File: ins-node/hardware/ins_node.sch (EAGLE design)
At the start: 11 parts, among them Q3 MOSFET-2N7000, U1 TINY85-20-DIP

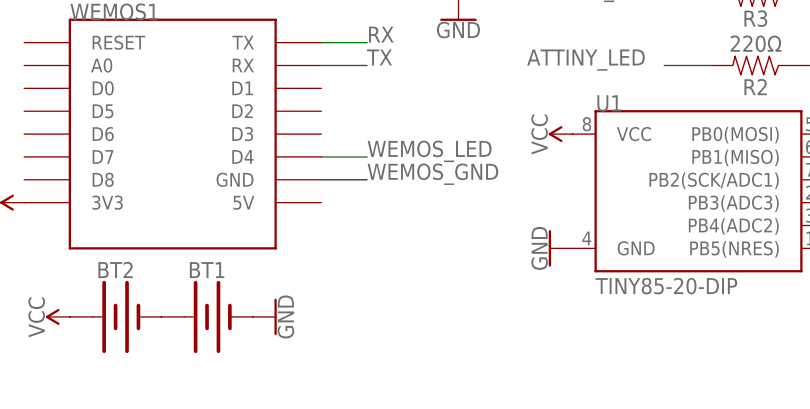
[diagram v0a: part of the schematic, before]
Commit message: Add decoupling capacitor
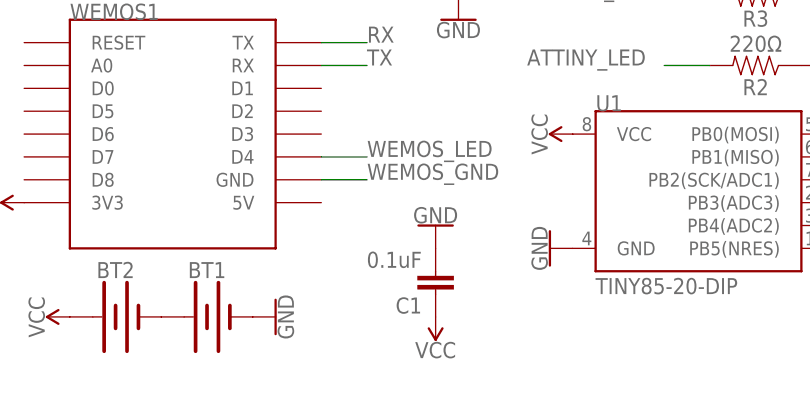
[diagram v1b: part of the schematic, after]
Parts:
- added C1: 0.1uF, SparkFun-Capacitors:0.1UF-KIT-EZ-50V-20%
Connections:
- net GND: now also C1.2
- net VCC: now also C1.1
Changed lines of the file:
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@@
 <part name="D2" library="SparkFun-LED" library_urn="urn:adsk.eagle:library:529" deviceset="LED" device="5MM-KIT" package3d_urn="urn:adsk.eagle:package:39357/1"/>
 <part name="GND5" library="SparkFun-PowerSymbols" library_urn="urn:adsk.eagle:library:530" deviceset="GND" device=""/>
+<part name="C1" library="SparkFun-Capacitors" library_urn="urn:adsk.eagle:library:510" deviceset="0.1UF" device="-KIT-EZ-50V-20%" package3d_urn="urn:adsk.eagle:package:37428/1" value="0.1uF"/>
+<part name="GND6" library="SparkFun-PowerSymbols" library_urn="urn:adsk.eagle:library:530" deviceset="GND" device=""/>
+<part name="SUPPLY5" library="SparkFun-PowerSymbols" library_urn="urn:adsk.eagle:library:530" deviceset="VCC" device=""/>
 </parts>
 <sheets>
@@
 <instance part="D2" gate="G$1" x="116.84" y="58.42" rot="R90"/>
 <instance part="GND5" gate="1" x="129.54" y="58.42" rot="R90"/>
+<instance part="C1" gate="G$1" x="73.66" y="35.56" rot="R180"/>
+<instance part="GND6" gate="1" x="73.66" y="40.64" rot="R180"/>
+<instance part="SUPPLY5" gate="G$1" x="73.66" y="30.48" rot="R180"/>
 </instances>
 <busses>
@@
 <wire x1="127" y1="58.42" x2="121.92" y2="58.42" width="0.1524" layer="91"/>
 </segment>
+<segment>
+<pinref part="C1" gate="G$1" pin="2"/>
+<pinref part="GND6" gate="1" pin="GND"/>
+</segment>
 </net>
 <net name="VCC" class="0">
@@
 <pinref part="SUPPLY4" gate="G$1" pin="VCC"/>
 </segment>
+<segment>
+<pinref part="C1" gate="G$1" pin="1"/>
+<pinref part="SUPPLY5" gate="G$1" pin="VCC"/>
+</segment>
 </net>

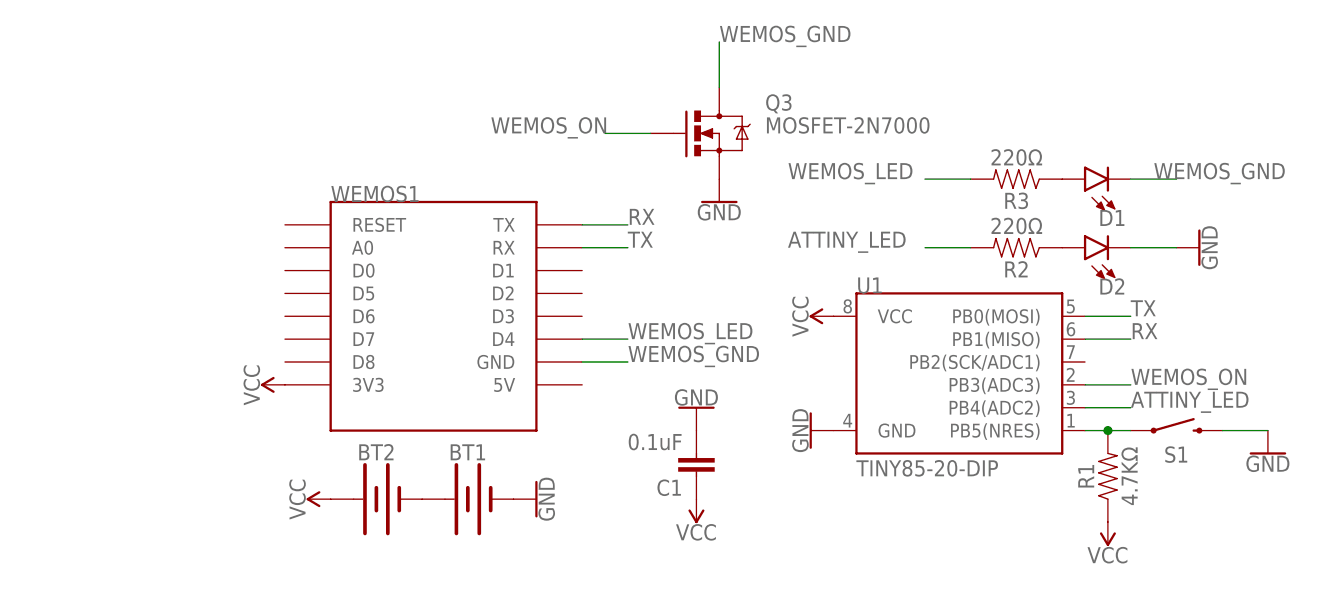
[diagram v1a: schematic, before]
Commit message: Fix wifi module powering issues
HW rev.1 includes:
* 2 MOSFETs for driving the wifi module
* 3 AAA batteries
* Additional decoupling capacitor
* Board restructuring as a result of new components

Fixes #29
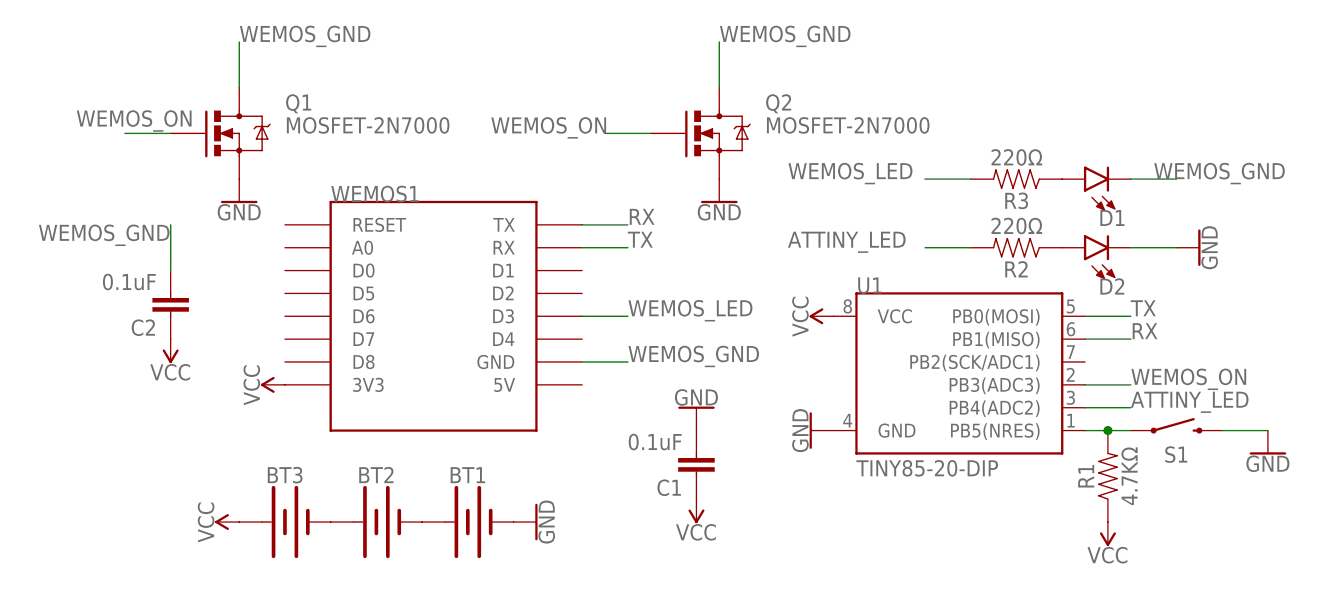
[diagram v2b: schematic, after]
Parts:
- added BT3: (no value), SparkFun-Batteries:BATTERY-AAA
- added C2: 0.1uF, SparkFun-Capacitors:0.1UF-KIT-EZ-50V-20%
- added Q1: MOSFET-2N7000, SparkFun-DiscreteSemi:MOSFET-NCHANNEL2N7000
- renumbered Q3 to Q2
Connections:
- new net N$5: BT2.+, BT3.-
- net GND: now also Q1.S
- net VCC: now also BT3.+, C2.1; no longer BT2.+
- net WEMOS_GND: now also C2.2, Q1.D
- net WEMOS_LED: now also WEMOS1.D3; no longer WEMOS1.D4
- net WEMOS_ON: now also Q1.G
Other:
- moved on the sheet: BT1, BT2
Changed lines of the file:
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@@
 <part name="WEMOS1" library="esp8266modules" deviceset="WEMOS-D1-MINI" device=""/>
 <part name="U1" library="SparkFun-Retired" library_urn="urn:adsk.eagle:library:533" deviceset="ATTINY45" device="TINY85-20-DIP" value="TINY85-20-DIP"/>
-<part name="Q3" library="SparkFun-DiscreteSemi" deviceset="MOSFET-NCHANNEL" device="2N7000" value="MOSFET-2N7000"/>
+<part name="Q2" library="SparkFun-DiscreteSemi" deviceset="MOSFET-NCHANNEL" device="2N7000" value="MOSFET-2N7000"/>
 <part name="BT2" library="SparkFun-Batteries" library_urn="urn:adsk.eagle:library:508" deviceset="BATTERY" device="-AAA" package3d_urn="urn:adsk.eagle:package:37212/1"/>
 <part name="BT1" library="SparkFun-Batteries" library_urn="urn:adsk.eagle:library:508" deviceset="BATTERY" device="-AAA" package3d_urn="urn:adsk.eagle:package:37212/1"/>
@@
 <part name="GND6" library="SparkFun-PowerSymbols" library_urn="urn:adsk.eagle:library:530" deviceset="GND" device=""/>
 <part name="SUPPLY5" library="SparkFun-PowerSymbols" library_urn="urn:adsk.eagle:library:530" deviceset="VCC" device=""/>
+<part name="BT3" library="SparkFun-Batteries" library_urn="urn:adsk.eagle:library:508" deviceset="BATTERY" device="-AAA" package3d_urn="urn:adsk.eagle:package:37212/1"/>
+<part name="Q1" library="SparkFun-DiscreteSemi" deviceset="MOSFET-NCHANNEL" device="2N7000" value="MOSFET-2N7000"/>
+<part name="GND7" library="SparkFun-PowerSymbols" library_urn="urn:adsk.eagle:library:530" deviceset="GND" device=""/>
+<part name="C2" library="SparkFun-Capacitors" library_urn="urn:adsk.eagle:library:510" deviceset="0.1UF" device="-KIT-EZ-50V-20%" package3d_urn="urn:adsk.eagle:package:37428/1" value="0.1uF"/>
+<part name="SUPPLY6" library="SparkFun-PowerSymbols" library_urn="urn:adsk.eagle:library:530" deviceset="VCC" device=""/>
 </parts>
 <sheets>
@@
 <instance part="WEMOS1" gate="D1" x="43.18" y="50.8"/>
 <instance part="U1" gate="G$1" x="104.14" y="43.18"/>
-<instance part="Q3" gate="G$1" x="76.2" y="71.12"/>
-<instance part="BT2" gate="G$1" x="38.1" y="30.48"/>
-<instance part="BT1" gate="G$1" x="48.26" y="30.48"/>
-<instance part="GND1" gate="1" x="55.88" y="30.48" rot="R90"/>
+<instance part="Q2" gate="G$1" x="76.2" y="71.12"/>
+<instance part="BT2" gate="G$1" x="38.1" y="27.94"/>
+<instance part="BT1" gate="G$1" x="48.26" y="27.94"/>
+<instance part="GND1" gate="1" x="55.88" y="27.94" rot="R90"/>
 <instance part="GND2" gate="1" x="76.2" y="63.5"/>
 <instance part="GND3" gate="1" x="86.36" y="38.1" rot="R270"/>
-<instance part="SUPPLY1" gate="G$1" x="33.02" y="30.48" rot="R90"/>
+<instance part="SUPPLY1" gate="G$1" x="22.86" y="27.94" rot="R90"/>
 <instance part="SUPPLY2" gate="G$1" x="27.94" y="43.18" rot="R90"/>
 <instance part="SUPPLY3" gate="G$1" x="88.9" y="50.8" rot="R90"/>
@@
 <instance part="GND6" gate="1" x="73.66" y="40.64" rot="R180"/>
 <instance part="SUPPLY5" gate="G$1" x="73.66" y="30.48" rot="R180"/>
+<instance part="BT3" gate="G$1" x="27.94" y="27.94"/>
+<instance part="Q1" gate="G$1" x="22.86" y="71.12"/>
+<instance part="GND7" gate="1" x="22.86" y="63.5"/>
+<instance part="C2" gate="G$1" x="15.24" y="53.34" rot="R180"/>
+<instance part="SUPPLY6" gate="G$1" x="15.24" y="48.26" rot="R180"/>
 </instances>
 <busses>
@@
 </segment>
 <segment>
-<pinref part="Q3" gate="G$1" pin="S"/>
+<pinref part="Q2" gate="G$1" pin="S"/>
 <pinref part="GND2" gate="1" pin="GND"/>
 </segment>
@@
 <pinref part="GND6" gate="1" pin="GND"/>
 </segment>
+<segment>
+<pinref part="Q1" gate="G$1" pin="S"/>
+<pinref part="GND7" gate="1" pin="GND"/>
+</segment>
 </net>
 <net name="VCC" class="0">
-<segment>
-<pinref part="BT2" gate="G$1" pin="+"/>
-<pinref part="SUPPLY1" gate="G$1" pin="VCC"/>
-</segment>
 <segment>
 <pinref part="WEMOS1" gate="D1" pin="3V3"/>
@@
 <pinref part="C1" gate="G$1" pin="1"/>
 <pinref part="SUPPLY5" gate="G$1" pin="VCC"/>
+</segment>
+<segment>
+<pinref part="SUPPLY1" gate="G$1" pin="VCC"/>
+<pinref part="BT3" gate="G$1" pin="+"/>
+</segment>
+<segment>
+<pinref part="C2" gate="G$1" pin="1"/>
+<pinref part="SUPPLY6" gate="G$1" pin="VCC"/>
 </segment>
 </net>
@@
 </segment>
 <segment>
-<pinref part="Q3" gate="G$1" pin="G"/>
+<pinref part="Q2" gate="G$1" pin="G"/>
 <wire x1="68.58" y1="71.12" x2="63.5" y2="71.12" width="0.1524" layer="91"/>
 <label x="50.8" y="71.12" size="1.778" layer="95"/>
+</segment>
+<segment>
+<pinref part="Q1" gate="G$1" pin="G"/>
+<wire x1="15.24" y1="71.12" x2="10.16" y2="71.12" width="0.1524" layer="91"/>
+<label x="17.78" y="73.66" size="1.778" layer="95" rot="R180"/>
 </segment>
 </net>
@@
 <net name="WEMOS_GND" class="0">
 <segment>
-<pinref part="Q3" gate="G$1" pin="D"/>
+<pinref part="Q2" gate="G$1" pin="D"/>
 <wire x1="76.2" y1="76.2" x2="76.2" y2="81.28" width="0.1524" layer="91"/>
 <label x="76.2" y="81.28" size="1.778" layer="95"/>
@@
 <wire x1="121.92" y1="66.04" x2="127" y2="66.04" width="0.1524" layer="91"/>
 <label x="124.46" y="66.04" size="1.778" layer="95"/>
+</segment>
+<segment>
+<pinref part="Q1" gate="G$1" pin="D"/>
+<wire x1="22.86" y1="76.2" x2="22.86" y2="81.28" width="0.1524" layer="91"/>
+<label x="22.86" y="81.28" size="1.778" layer="95"/>
+</segment>
+<segment>
+<pinref part="C2" gate="G$1" pin="2"/>
+<wire x1="15.24" y1="55.88" x2="15.24" y2="60.96" width="0.1524" layer="91"/>
+<label x="15.24" y="60.96" size="1.778" layer="95" rot="R180"/>
 </segment>
 </net>
@@
 <net name="WEMOS_LED" class="0">
 <segment>
-<pinref part="WEMOS1" gate="D1" pin="D4"/>
-<wire x1="60.96" y1="48.26" x2="66.04" y2="48.26" width="0.1524" layer="91"/>
-<label x="66.04" y="48.26" size="1.778" layer="95"/>
+<label x="66.04" y="50.8" size="1.778" layer="95"/>
+<pinref part="WEMOS1" gate="D1" pin="D3"/>
+<wire x1="60.96" y1="50.8" x2="66.04" y2="50.8" width="0.1524" layer="91"/>
 </segment>
 <segment>
@@
 </segment>
 </net>
+<net name="N$5" class="0">
+<segment>
+<pinref part="BT2" gate="G$1" pin="+"/>
+<pinref part="BT3" gate="G$1" pin="-"/>
+</segment>
+</net>

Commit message: Add pulldown resistor for MOSFETs base
Add a pulldown resistor for the MOSFET trigger pins so to make sure
that we have a clean signal that only activates the Wifi module
when we want.

This change constitutes HW Rev. 2
Fixes #71
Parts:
- added R4: 4.7KΩ, SparkFun-Resistors:RESISTORAXIAL-0.3
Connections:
- net GND: now also R4.1
- net WEMOS_ON: now also R4.2
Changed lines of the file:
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@@
 <?xml version="1.0" encoding="utf-8"?>
 <!DOCTYPE eagle SYSTEM "eagle.dtd">
-<eagle version="8.3.0">
+<eagle version="8.4.3">
 <drawing>
 <settings>
@@
 <part name="C2" library="SparkFun-Capacitors" library_urn="urn:adsk.eagle:library:510" deviceset="0.1UF" device="-KIT-EZ-50V-20%" package3d_urn="urn:adsk.eagle:package:37428/1" value="0.1uF"/>
 <part name="SUPPLY6" library="SparkFun-PowerSymbols" library_urn="urn:adsk.eagle:library:530" deviceset="VCC" device=""/>
+<part name="R4" library="SparkFun-Resistors" library_urn="urn:adsk.eagle:library:532" deviceset="RESISTOR" device="AXIAL-0.3" package3d_urn="urn:adsk.eagle:package:39658/1" value="4.7KΩ"/>
 </parts>
 <sheets>
@@
 <instance part="C2" gate="G$1" x="15.24" y="53.34" rot="R180"/>
 <instance part="SUPPLY6" gate="G$1" x="15.24" y="48.26" rot="R180"/>
+<instance part="R4" gate="G$1" x="50.8" y="78.74" rot="R180"/>
 </instances>
 <busses>
@@
 <pinref part="GND7" gate="1" pin="GND"/>
 </segment>
+<segment>
+<pinref part="R4" gate="G$1" pin="1"/>
+<wire x1="55.88" y1="78.74" x2="63.5" y2="78.74" width="0.1524" layer="91"/>
+<label x="63.5" y="78.74" size="1.778" layer="95"/>
+</segment>
 </net>
 <net name="VCC" class="0">
@@
 <label x="17.78" y="73.66" size="1.778" layer="95" rot="R180"/>
 </segment>
-</net>
+<segment>
+<pinref part="R4" gate="G$1" pin="2"/>
+<wire x1="45.72" y1="78.74" x2="40.64" y2="78.74" width="0.1524" layer="91"/>
+<label x="30.48" y="76.2" size="1.778" layer="95"/>
+</segment>
+</net>
